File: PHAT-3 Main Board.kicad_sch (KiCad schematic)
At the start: 9 parts, among them U1 AHT21, U2 ESP32-S3 Dual-core SX1262, U3 BME280, U4 GY-521 MPU-6050, U5 LM2596, U6 GT-7U, U7 SCD41, U8 uCAM-III

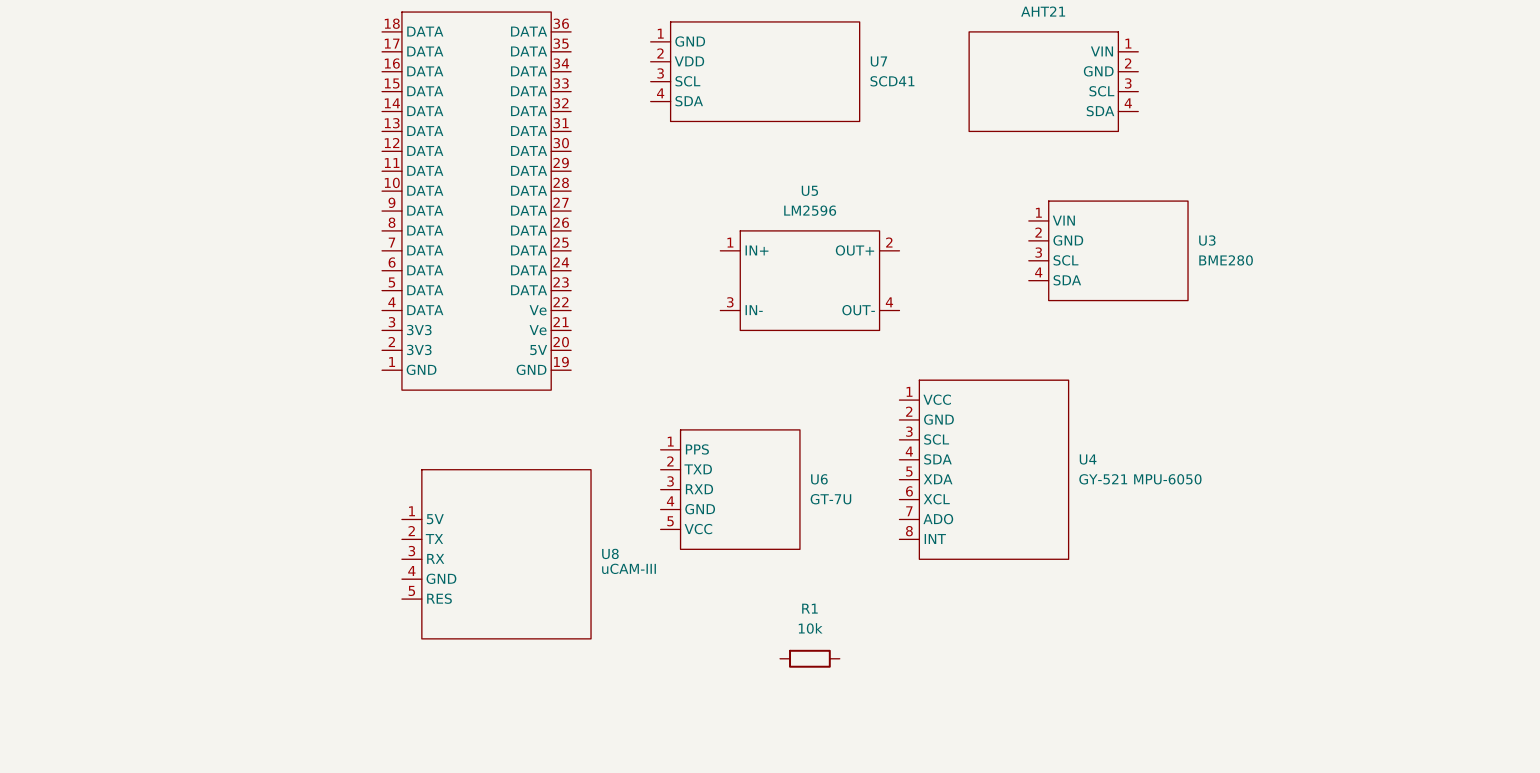
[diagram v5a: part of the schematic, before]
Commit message: Added SD Card Reader
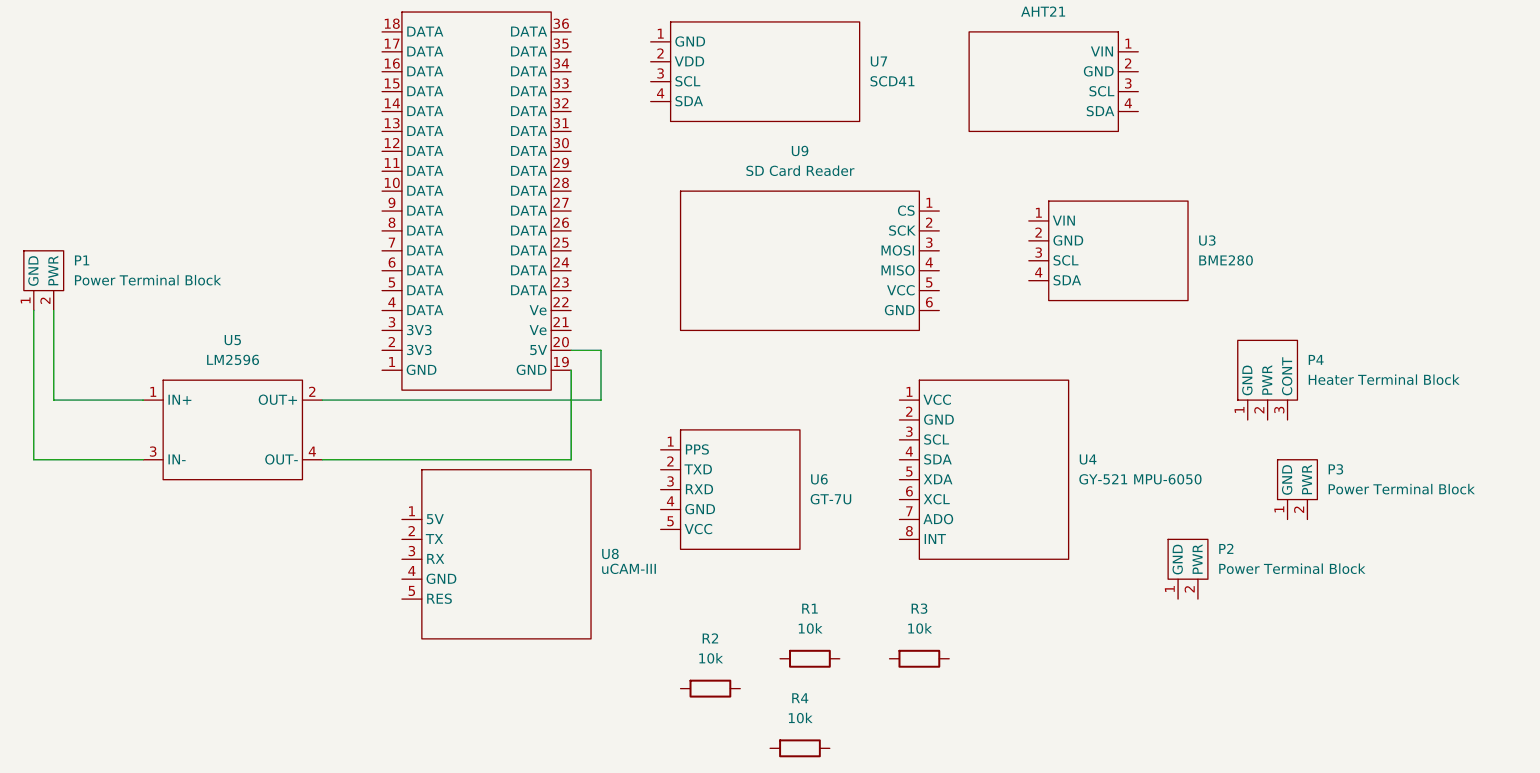
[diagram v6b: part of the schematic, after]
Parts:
- added P1, P2, P3: Power Terminal Block, TerminalBlock_Phoenix:TerminalBlock_Phoenix_MKDS-1,5-2-5.08_1x02_P5.08mm_Horizontal, symbol Footprint Library:Power_Terminal_Block
- added P4: Heater Terminal Block, TerminalBlock_Phoenix:TerminalBlock_Phoenix_MKDS-1,5-3-5.08_1x03_P5.08mm_Horizontal, symbol Footprint Library:Heater_Terminal_Block
- added R2, R3, R4: 10k, Resistor_THT:R_Axial_DIN0207_L6.3mm_D2.5mm_P10.16mm_Horizontal, symbol Device:R
- added U9: SD Card Reader, Actual Footprint Library:SD Card Reader, symbol Footprint Library:SD_Card_Reader
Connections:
- net at U5.1 (IN+): now also P1.2 (PWR)
- net at U5.2 (OUT+): now also U2.20 (5V)
- net at U5.3 (IN-): now also P1.1 (GND)
- net at U5.4 (OUT-): now also U2.19 (GND)
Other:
- moved on the sheet: U5

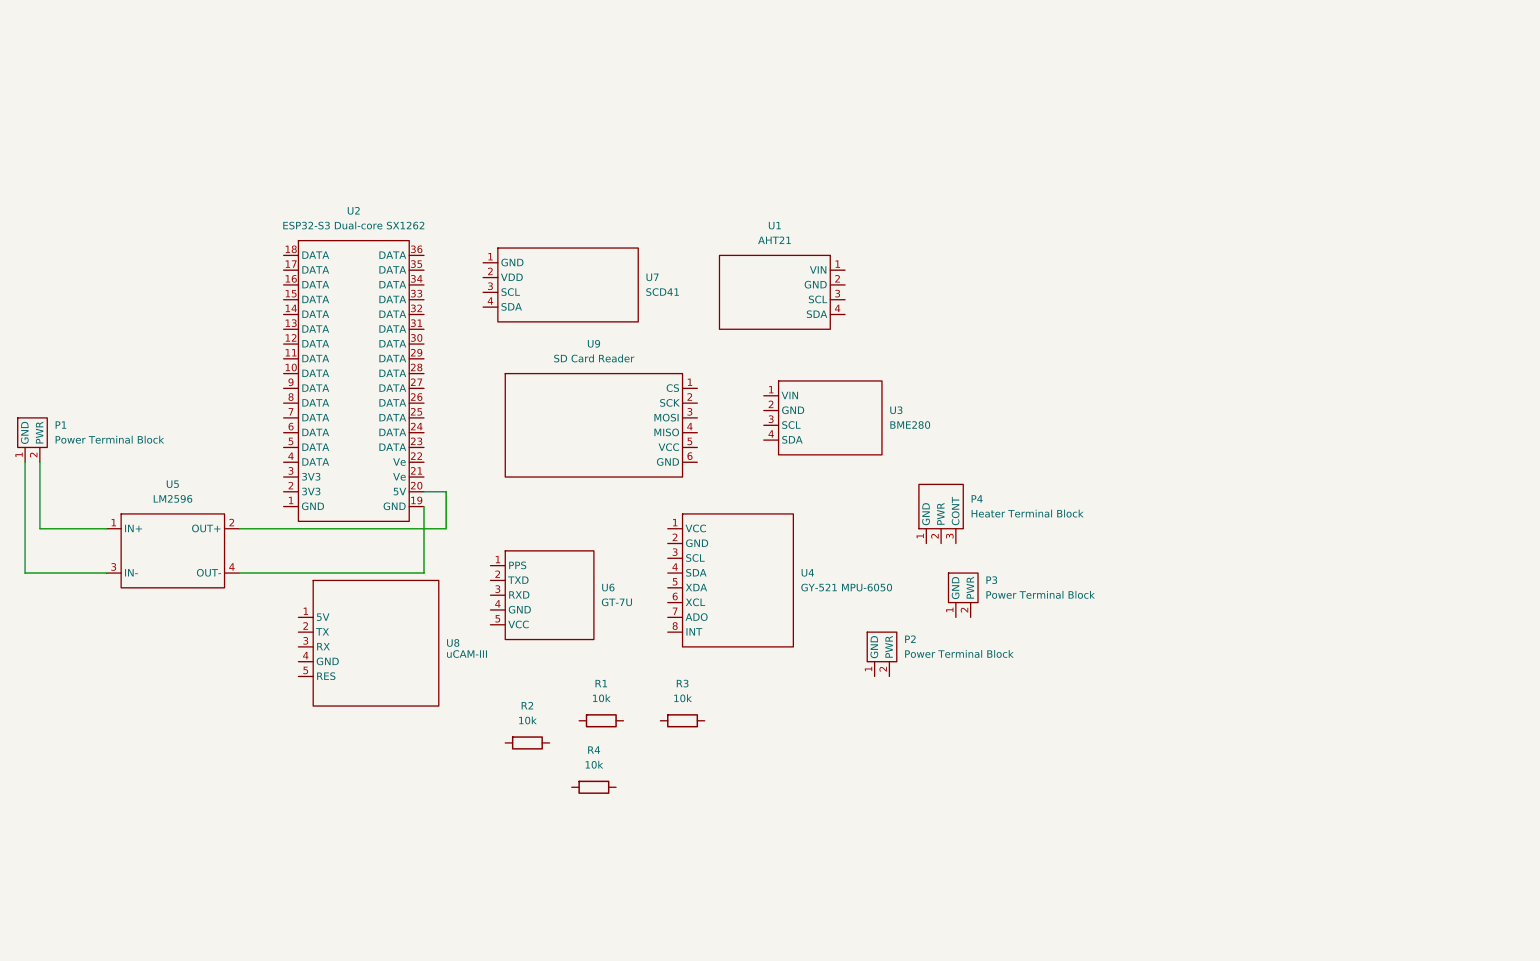
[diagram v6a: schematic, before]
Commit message: Added logic Level Converter and Relay
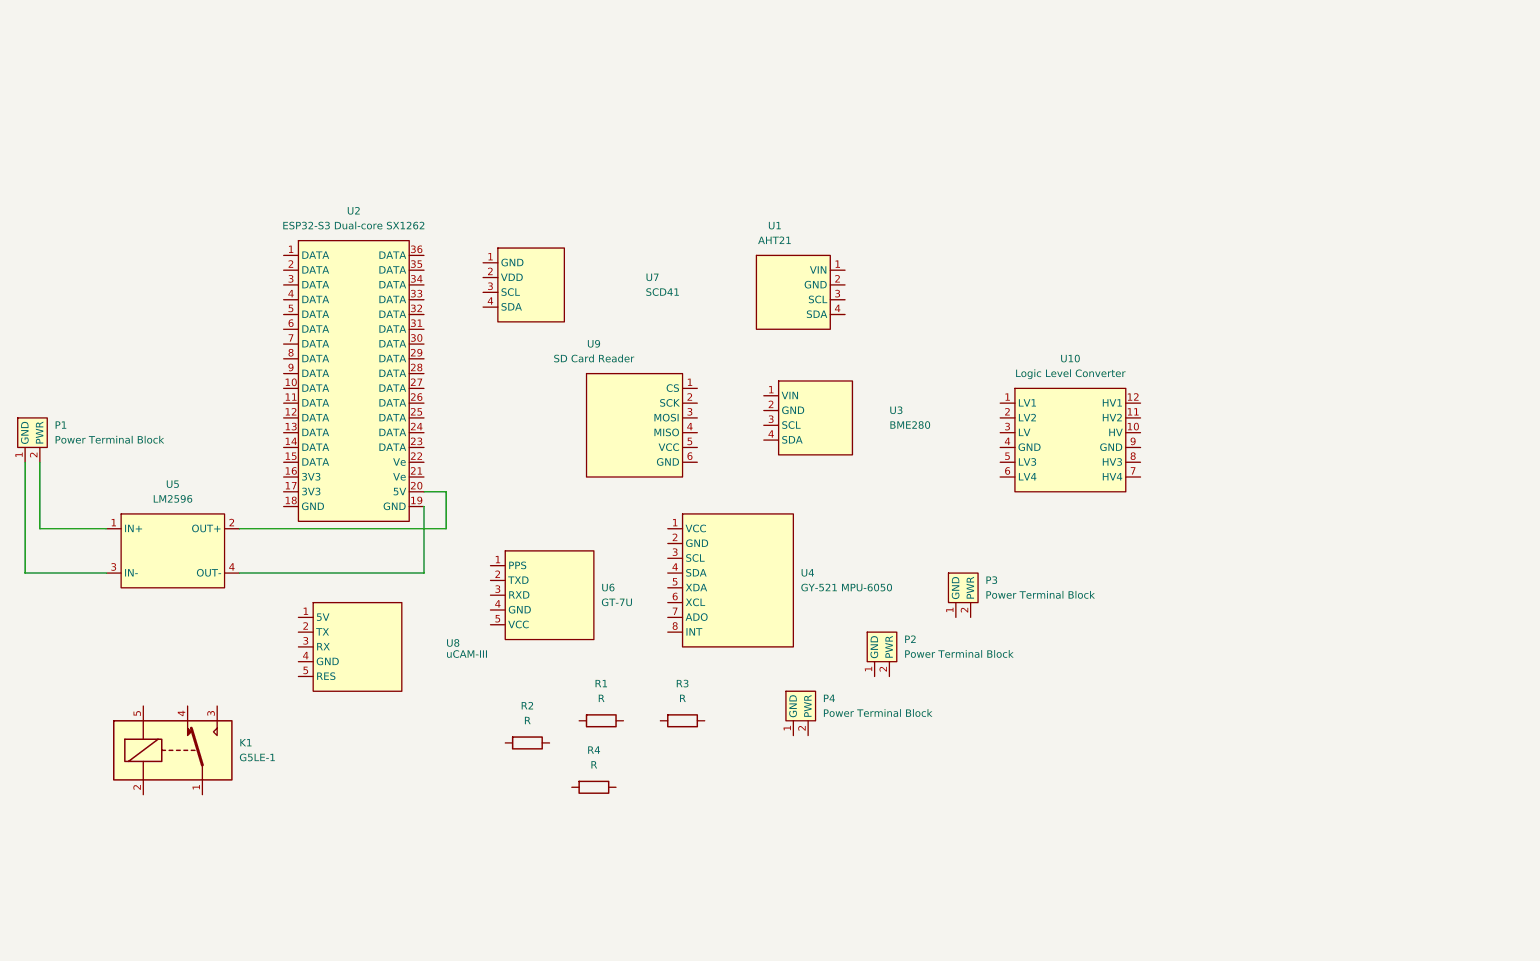
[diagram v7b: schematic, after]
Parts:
- removed P4: Heater Terminal Block, TerminalBlock_Phoenix:TerminalBlock_Phoenix_MKDS-1,5-3-5.08_1x03_P5.08mm_Horizontal, symbol Footprint Library:Heater_Terminal_Block
- added K1: G5LE-1, Relay_THT:Relay_SPDT_Omron-G5LE-1, symbol Relay:G5LE-1
- added P4: Power Terminal Block, TerminalBlock_Phoenix:TerminalBlock_Phoenix_MKDS-1,5-2-5.08_1x02_P5.08mm_Horizontal, symbol Footprint Library:Power_Terminal_Block
- added U10: Logic Level Converter, Actual Footprint Library:Logic Level Converter, symbol Footprint Library:Logic_Level_Converter
- R1, R2, R3, R4: value 10k -> R
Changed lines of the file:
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@@
 			)
 		)
-		(property "Value" "10k"
+		(property "Value" "R"
 			(at 113.03 140.97 90)
 			(effects
@@
 			)
 		)
-		(property "Value" "10k"
+		(property "Value" "R"
 			(at 139.7 137.16 90)
 			(effects
@@
 	)
 	(symbol
-		(lib_id "Footprint Library:Heater_Terminal_Block")
-		(at 184.15 107.95 0)
-		(unit 1)
-		(exclude_from_sim no)
-		(in_bom yes)
-		(on_board yes)
-		(dnp no)
-		(fields_autoplaced yes)
-		(property "Reference" "P4"
-			(at 189.23 102.8699 0)
-			(effects
-				(font
-					(size 1.27 1.27)
-				)
-				(justify left)
-			)
-		)
-		(property "Value" "Heater Terminal Block"
-			(at 189.23 105.4099 0)
-			(effects
-				(font
-					(size 1.27 1.27)
-				)
-				(justify left)
-			)
-		)
-		(property "Footprint" "TerminalBlock_Phoenix:TerminalBlock_Phoenix_MKDS-1,5-3-5.08_1x03_P5.08mm_Horizontal"
-			(at 184.404 98.298 0)
+		(lib_id "Footprint Library:Logic_Level_Converter")
+		(at 196.85 99.06 0)
+		(unit 1)
+		(exclude_from_sim no)
+		(in_bom yes)
+		(on_board yes)
+		(dnp no)
+		(fields_autoplaced yes)
+		(property "Reference" "U10"
+			(at 206.375 78.74 0)
+			(effects
+				(font
+					(size 1.27 1.27)
+				)
+			)
+		)
+		(property "Value" "Logic Level Converter"
+			(at 206.375 81.28 0)
+			(effects
+				(font
+					(size 1.27 1.27)
+				)
+			)
+		)
+		(property "Footprint" "Actual Footprint Library:Logic Level Converter"
+			(at 196.85 102.87 0)
 			(effects
 				(font
@@
 		)
 		(property "Datasheet" ""
-			(at 184.15 107.95 0)
+			(at 196.85 102.87 0)
 			(effects
 				(font
@@
 		)
 		(property "Description" ""
-			(at 184.15 107.95 0)
-			(effects
-				(font
-					(size 1.27 1.27)
-				)
-				(hide yes)
-			)
-		)
-		(pin "1"
-		)
-		(pin "2"
+			(at 196.85 102.87 0)
+			(effects
+				(font
+					(size 1.27 1.27)
+				)
+				(hide yes)
+			)
+		)
+		(pin "11"
+		)
+		(pin "8"
+		)
+		(pin "9"
+		)
+		(pin "4"
+		)
+		(pin "6"
+		)
+		(pin "5"
+		)
+		(pin "10"
+		)
+		(pin "12"
+		)
+		(pin "1"
 		)
 		(pin "3"
 		)
+		(pin "2"
+		)
+		(pin "7"
+		)
 		(instances
 			(project ""
 				(path "/da389c8a-9ca2-41c4-a7eb-3ce46ba4333b"
-					(reference "P4")
+					(reference "U10")
 					(unit 1)
 				)
@@
 			)
 		)
-		(property "Value" "10k"
+		(property "Value" "R"
 			(at 124.46 148.59 90)
 			(effects
@@
 	(symbol
 		(lib_id "Footprint Library:Power_Terminal_Block")
+		(at 158.75 140.97 0)
+		(unit 1)
+		(exclude_from_sim no)
+		(in_bom yes)
+		(on_board yes)
+		(dnp no)
+		(fields_autoplaced yes)
+		(property "Reference" "P4"
+			(at 163.83 137.1599 0)
+			(effects
+				(font
+					(size 1.27 1.27)
+				)
+				(justify left)
+			)
+		)
+		(property "Value" "Power Terminal Block"
+			(at 163.83 139.6999 0)
+			(effects
+				(font
+					(size 1.27 1.27)
+				)
+				(justify left)
+			)
+		)
+		(property "Footprint" "TerminalBlock_Phoenix:TerminalBlock_Phoenix_MKDS-1,5-2-5.08_1x02_P5.08mm_Horizontal"
+			(at 158.75 133.858 0)
+			(effects
+				(font
+					(size 1.27 1.27)
+				)
+				(hide yes)
+			)
+		)
+		(property "Datasheet" ""
+			(at 158.75 140.97 0)
+			(effects
+				(font
+					(size 1.27 1.27)
+				)
+				(hide yes)
+			)
+		)
+		(property "Description" ""
+			(at 158.75 140.97 0)
+			(effects
+				(font
+					(size 1.27 1.27)
+				)
+				(hide yes)
+			)
+		)
+		(pin "2"
+		)
+		(pin "1"
+		)
+		(instances
+			(project ""
+				(path "/da389c8a-9ca2-41c4-a7eb-3ce46ba4333b"
+					(reference "P4")
+					(unit 1)
+				)
+			)
+		)
+	)
+	(symbol
+		(lib_id "Relay:G5LE-1")
+		(at 52.07 146.05 0)
+		(unit 1)
+		(exclude_from_sim no)
+		(in_bom yes)
+		(on_board yes)
+		(dnp no)
+		(fields_autoplaced yes)
+		(property "Reference" "K1"
+			(at 63.5 144.7799 0)
+			(effects
+				(font
+					(size 1.27 1.27)
+				)
+				(justify left)
+			)
+		)
+		(property "Value" "G5LE-1"
+			(at 63.5 147.3199 0)
+			(effects
+				(font
+					(size 1.27 1.27)
+				)
+				(justify left)
+			)
+		)
+		(property "Footprint" "Relay_THT:Relay_SPDT_Omron-G5LE-1"
+			(at 63.5 147.32 0)
+			(effects
+				(font
+					(size 1.27 1.27)
+				)
+				(justify left)
+				(hide yes)
+			)
+		)
+		(property "Datasheet" "http://www.omron.com/ecb/products/pdf/en-g5le.pdf"
+			(at 52.07 146.05 0)
+			(effects
+				(font
+					(size 1.27 1.27)
+				)
+				(hide yes)
+			)
+		)
+		(property "Description" "Omron G5LE relay, Miniature Single Pole, SPDT, 10A"
+			(at 52.07 146.05 0)
+			(effects
+				(font
+					(size 1.27 1.27)
+				)
+				(hide yes)
+			)
+		)
+		(pin "1"
+		)
+		(pin "5"
+		)
+		(pin "2"
+		)
+		(pin "3"
+		)
+		(pin "4"
+		)
+		(instances
+			(project ""
+				(path "/da389c8a-9ca2-41c4-a7eb-3ce46ba4333b"
+					(reference "K1")
+					(unit 1)
+				)
+			)
+		)
+	)
+	(symbol
+		(lib_id "Footprint Library:Power_Terminal_Block")
 		(at 172.72 130.81 0)
 		(unit 1)
@@
 			)
 		)
-		(property "Value" "10k"
+		(property "Value" "R"
 			(at 125.73 137.16 90)
 			(effects

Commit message: Tried Wiring Everything
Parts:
- removed R3, R4: R, Resistor_THT:R_Axial_DIN0207_L6.3mm_D2.5mm_P10.16mm_Horizontal, symbol Device:R
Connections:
- net at U6.2 (TXD): now also U2.36 (U1RTS)
- net at U6.3 (RXD): now also U2.35 (U1CTS)
- net GND: now reaches U6.4 (GND)
- net GND: now also P1.1 (GND), U1.2 (GND), U10.4 (GND), U10.9 (GND), U2.19 (GND), U3.2 (GND), U4.2 (GND), U5.3 (IN-), U5.4 (OUT-), U7.1 (GND), U8.4 (GND)
- net at U6.5 (VCC): now also U1.1 (VIN), U10.10 (HV), U2.20 (5V), U3.1 (VIN), U4.1 (VCC), U5.2 (OUT+), U7.2 (VDD), U8.1 (5V)
- net at U8.2 (TX): now also U2.23 (U0RXD)
- net at U8.3 (RX): now also U2.24 (U0TXD)
- net at U4.3 (SCL): now also U1.3 (SCL), U10.12 (HV1), U3.3 (SCL), U7.3 (SCL)
- net at U4.4 (SDA): now also U1.4 (SDA), U10.11 (HV2), U3.4 (SDA), U7.4 (SDA)
- net at U2.22 (Ve): now also U10.3 (LV)
- net at U2.27 (DATA): now also U10.2 (LV2)
- net at U2.28 (DATA): now also U10.1 (LV1)
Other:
- moved on the sheet: P1, P2, P3, P4, R2, U10, U2, U4, U5, U6
